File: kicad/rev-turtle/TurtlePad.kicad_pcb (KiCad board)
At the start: 2 copper layers, 57.2 x 63.6 mm, 40 parts, among them J1 USB_IN, J2 AVR-ISP-6, SW1 SW_Push, U1 USBLC6-2SC6, U2 ATMEGA32U4, Y1 16MHz

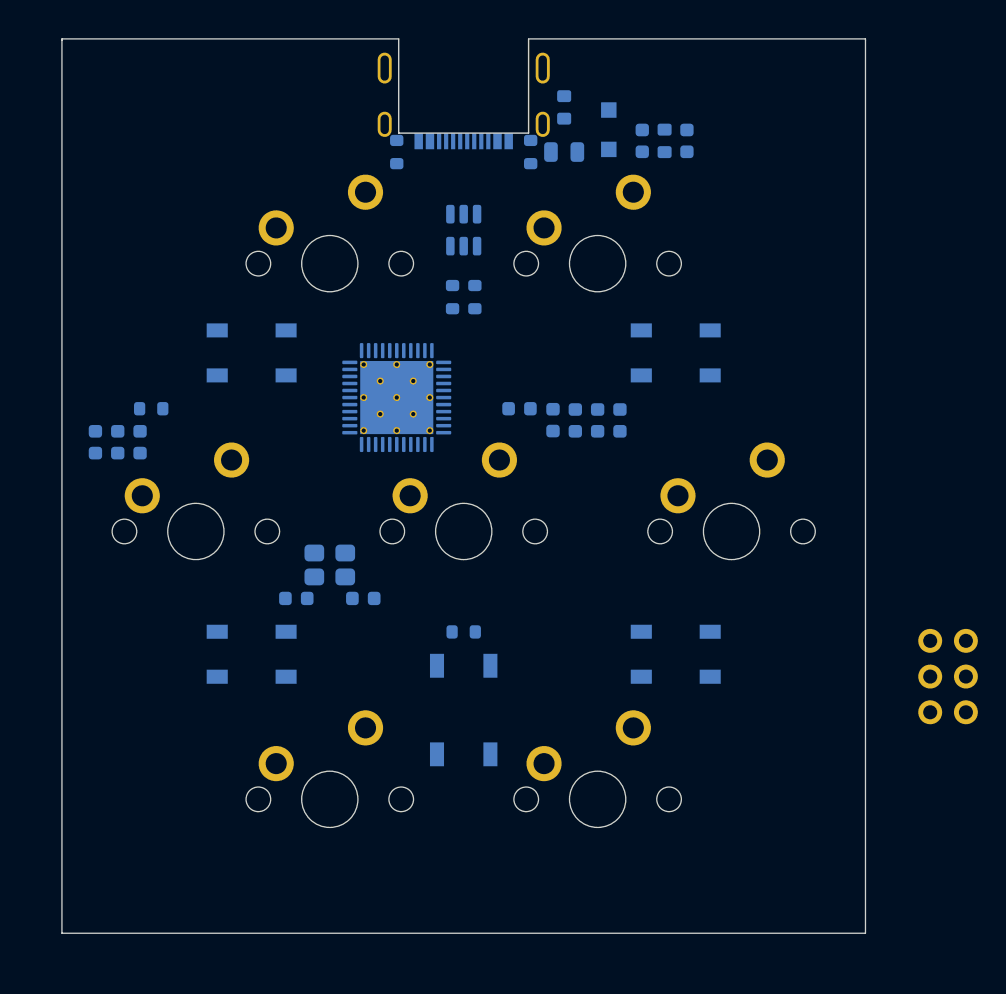
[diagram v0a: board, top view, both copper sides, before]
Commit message: Placed and routed all components on PCB
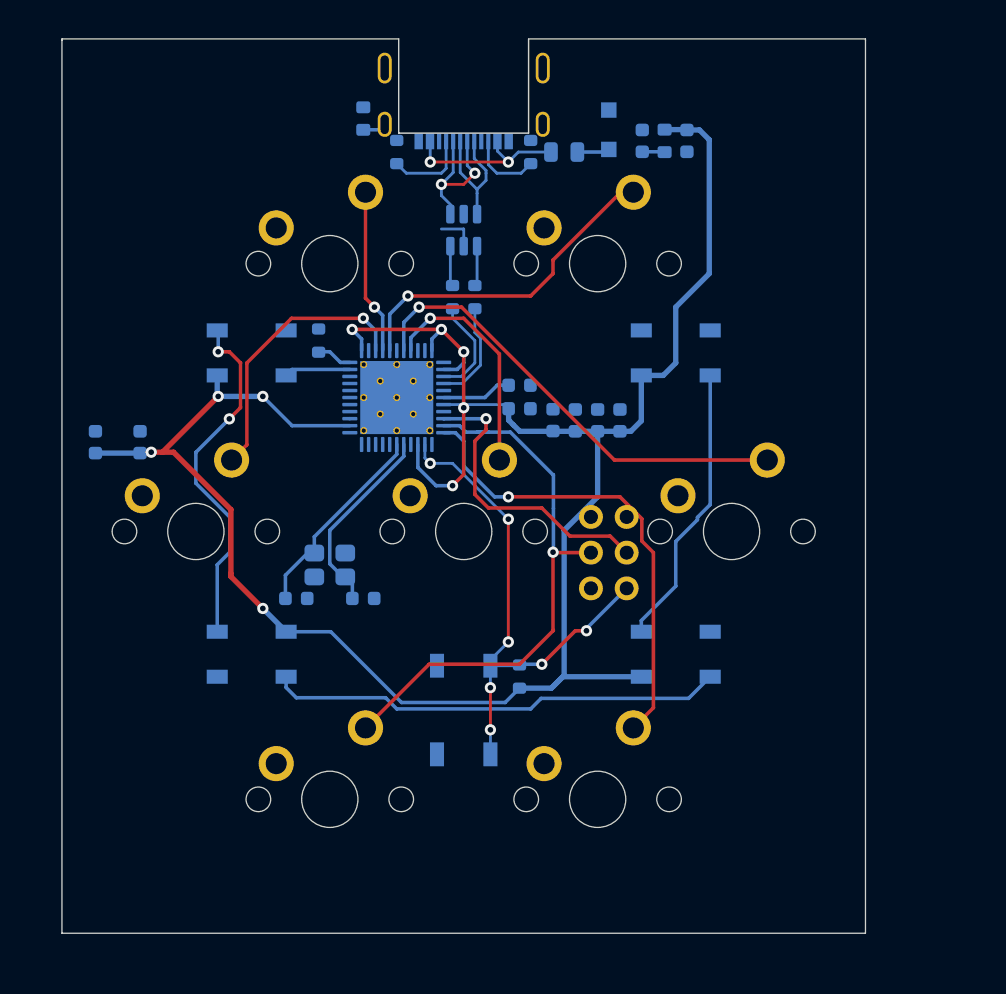
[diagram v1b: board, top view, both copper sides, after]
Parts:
- moved C9 28.9 mm to (131.8, 79.4), turned to 0 degrees
- moved J2 25.7 mm to (138.1, 91.3)
- moved FB2 14.3 mm to (120.7, 60.4)
- moved R6 12.9 mm to (117.5, 76.2), turned to -90 degrees
- moved R5 5.08 mm to (131.8, 100.1), turned to -90 degrees
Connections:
- J2 pad 1: MISO -> MX7
- J2 pad 4: MOSI -> MX6
- U2 pad 10: MOSI -> MX6
- U2 pad 11: MISO -> MX7
- U2 pad 18: MX1 -> unconnected-(U2-Pad18)
- U2 pad 19: MX2 -> unconnected-(U2-Pad19)
- U2 pad 20: MX3 -> SCK
- U2 pad 21: MX4 -> MOSI
- U2 pad 22: MX6 -> unconnected-(U2-Pad22)
- U2 pad 25: MX5 -> MISO
- U2 pad 26: MX7 -> unconnected-(U2-Pad26)
- U2 pad 32: unconnected-(U2-Pad32) -> LED
- U2 pad 36: unconnected-(U2-Pad36) -> MX3
- U2 pad 37: unconnected-(U2-Pad37) -> MX1
- U2 pad 38: unconnected-(U2-Pad38) -> MX2
- U2 pad 40: unconnected-(U2-Pad40) -> MX5
- U2 pad 41: unconnected-(U2-Pad41) -> MX4
- U2 pad 8: LED -> unconnected-(U2-Pad8)
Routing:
- net VCC: track 0.00 -> 157.7 mm, vias 0 -> 9
- net MX6: track 0.00 -> 40.1 mm, vias 0 -> 1
- net RST: track 0.00 -> 38.0 mm, vias 0 -> 7
- net MX7: track 0.00 -> 33.5 mm, vias 0 -> 1
- net MX5: track 0.00 -> 32.8 mm, vias 0 -> 1
- net Net-(RGB2-Pad2): track 0.00 -> 32.5 mm
- net Net-(RGB1-Pad2): track 0.00 -> 25.3 mm, vias 0 -> 2
- net MX2: track 0.00 -> 24.1 mm, vias 0 -> 1
- net SCK: track 0.00 -> 21.2 mm, vias 0 -> 1
- net Net-(RGB3-Pad2): track 0.00 -> 20.3 mm
- net MX3: track 0.00 -> 19.6 mm, vias 0 -> 1
- net MX4: track 0.00 -> 16.4 mm, vias 0 -> 1
- net /VBUS: track 0.00 -> 15.0 mm, vias 0 -> 2
- net Net-(C8-Pad2): track 0.00 -> 14.5 mm
- net Net-(C7-Pad2): track 0.00 -> 13.9 mm
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
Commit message: PCB edge and copper fill
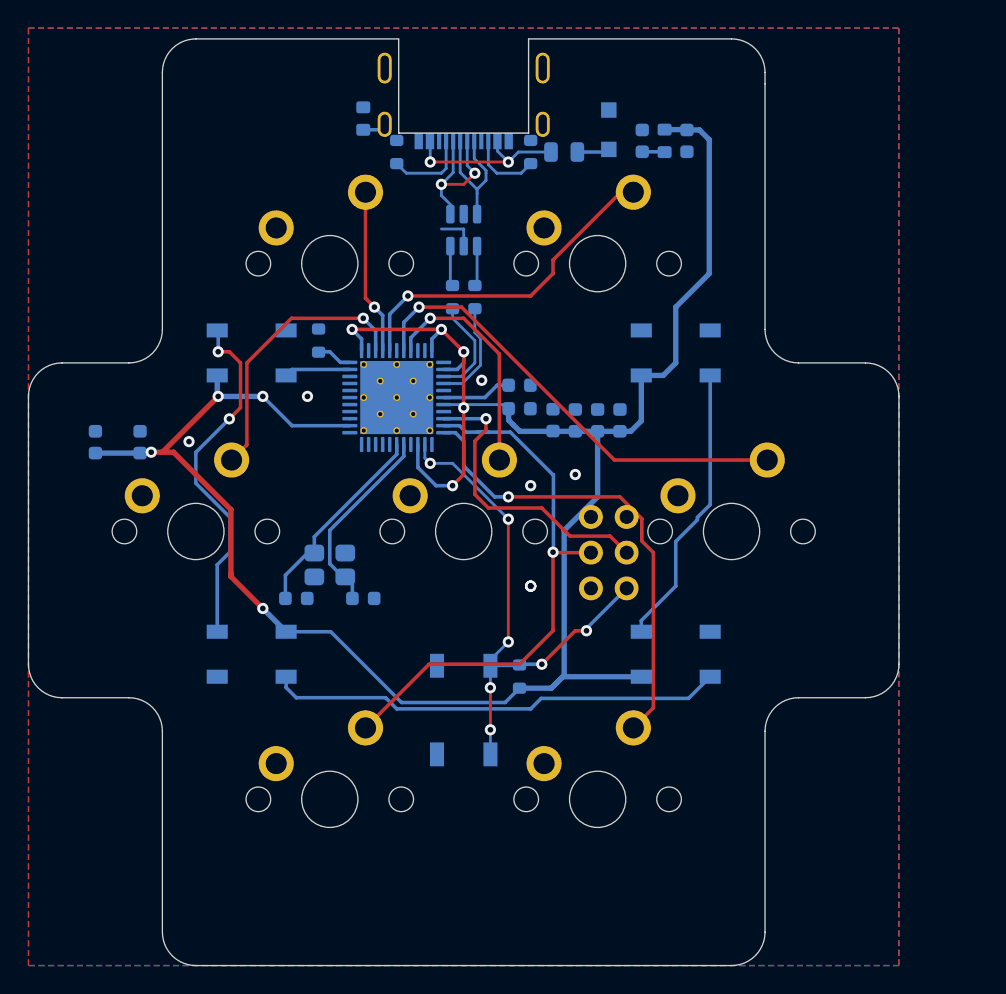
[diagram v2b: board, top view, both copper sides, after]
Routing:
- net GND: vias 0 -> 8
- added copper zone on B.Cu, net GND
- added copper zone on F.Cu, net GND
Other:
- board size 57.2 x 63.6 mm -> 61.9 x 65.9 mm
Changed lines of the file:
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@@
     )
   )
-  (gr_line (start 156.36875 118.350939) (end 99.21875 118.350939) (layer "Edge.Cuts") (width 0.05))
-  (gr_line (start 99.21875 54.742189) (end 99.21875 54.850939) (layer "Edge.Cuts") (width 0.05))
-  (gr_line (start 99.21875 118.350939) (end 99.21875 54.850939) (layer "Edge.Cuts") (width 0.05))
-  (gr_line (start 132.40875 54.742189) (end 156.36875 54.742189) (layer "Edge.Cuts") (width 0.05))
-  (gr_line (start 156.36875 54.850939) (end 156.36875 54.742189) (layer "Edge.Cuts") (width 0.05))
-  (gr_line (start 123.16875 54.742189) (end 99.21875 54.742189) (layer "Edge.Cuts") (width 0.05))
-  (gr_line (start 156.36875 54.850939) (end 156.36875 118.350939) (layer "Edge.Cuts") (width 0.05))
+  (gr_arc (start 156.36875 77.7875) (mid 158.052548 78.484952) (end 158.75 80.16875) (layer "Edge.Cuts") (width 0.05))
+  (gr_arc (start 106.3625 57.123439) (mid 107.059952 55.439641) (end 108.74375 54.742189) (layer "Edge.Cuts") (width 0.05))
+  (gr_arc (start 103.98125 101.6) (mid 105.665048 102.297452) (end 106.3625 103.98125) (layer "Edge.Cuts") (width 0.05))
+  (gr_line (start 149.225 57.94375) (end 149.225 57.123439) (layer "Edge.Cuts") (width 0.05))
+  (gr_arc (start 146.84375 54.742189) (mid 148.527548 55.439641) (end 149.225 57.123439) (layer "Edge.Cuts") (width 0.05))
+  (gr_line (start 156.36875 77.7875) (end 151.60625 77.7875) (layer "Edge.Cuts") (width 0.05))
+  (gr_arc (start 151.60625 77.7875) (mid 149.922452 77.090048) (end 149.225 75.40625) (layer "Edge.Cuts") (width 0.05))
+  (gr_arc (start 99.21875 101.6) (mid 97.534952 100.902548) (end 96.8375 99.21875) (layer "Edge.Cuts") (width 0.05))
+  (gr_line (start 99.21875 101.6) (end 103.98125 101.6) (layer "Edge.Cuts") (width 0.05))
+  (gr_line (start 108.74375 120.65) (end 146.84375 120.65) (layer "Edge.Cuts") (width 0.05))
+  (gr_line (start 106.3625 57.123439) (end 106.3625 75.40625) (layer "Edge.Cuts") (width 0.05))
+  (gr_line (start 149.225 118.26875) (end 149.225 103.98125) (layer "Edge.Cuts") (width 0.05))
+  (gr_line (start 106.3625 103.98125) (end 106.3625 118.26875) (layer "Edge.Cuts") (width 0.05))
+  (gr_line (start 103.98125 77.7875) (end 99.21875 77.7875) (layer "Edge.Cuts") (width 0.05))
+  (gr_line (start 158.75 99.21875) (end 158.75 80.16875) (layer "Edge.Cuts") (width 0.05))
+  (gr_arc (start 158.75 99.21875) (mid 158.052548 100.902548) (end 156.36875 101.6) (layer "Edge.Cuts") (width 0.05))
+  (gr_arc (start 149.225 103.98125) (mid 149.922452 102.297452) (end 151.60625 101.6) (layer "Edge.Cuts") (width 0.05))
+  (gr_arc (start 149.225 118.26875) (mid 148.527548 119.952548) (end 146.84375 120.65) (layer "Edge.Cuts") (width 0.05))
+  (gr_arc (start 96.8375 80.16875) (mid 97.534952 78.484952) (end 99.21875 77.7875) (layer "Edge.Cuts") (width 0.05))
+  (gr_line (start 151.60625 101.6) (end 156.36875 101.6) (layer "Edge.Cuts") (width 0.05))
+  (gr_line (start 123.16875 54.742189) (end 108.74375 54.742189) (layer "Edge.Cuts") (width 0.05))
+  (gr_line (start 96.8375 80.16875) (end 96.8375 99.21875) (layer "Edge.Cuts") (width 0.05))
+  (gr_line (start 149.225 75.40625) (end 149.225 57.94375) (layer "Edge.Cuts") (width 0.05))
+  (gr_arc (start 108.74375 120.65) (mid 107.059952 119.952548) (end 106.3625 118.26875) (layer "Edge.Cuts") (width 0.05))
+  (gr_arc (start 106.3625 75.40625) (mid 105.665048 77.090048) (end 103.98125 77.7875) (layer "Edge.Cuts") (width 0.05))
+  (gr_line (start 132.40875 54.742189) (end 146.84375 54.742189) (layer "Edge.Cuts") (width 0.05))
+  (via (at 132.55625 93.6625) (size 0.8) (drill 0.4) (layers "F.Cu" "B.Cu") (free) (net 2))
+  (via (at 135.73125 85.725) (size 0.8) (drill 0.4) (layers "F.Cu" "B.Cu") (free) (net 2))
+  (via (at 132.55625 93.6625) (size 0.8) (drill 0.4) (layers "F.Cu" "B.Cu") (free) (net 2))
+  (via (at 129.072531 79.023114) (size 0.8) (drill 0.4) (layers "F.Cu" "B.Cu") (free) (net 2))
+  (via (at 108.254941 83.381183) (size 0.8) (drill 0.4) (layers "F.Cu" "B.Cu") (free) (net 2))
+  (via (at 132.55625 93.6625) (size 0.8) (drill 0.4) (layers "F.Cu" "B.Cu") (free) (net 2))
+  (via (at 116.68125 80.16875) (size 0.8) (drill 0.4) (layers "F.Cu" "B.Cu") (free) (net 2))
+  (via (at 132.55625 86.51875) (size 0.8) (drill 0.4) (layers "F.Cu" "B.Cu") (free) (net 2))
   (segment (start 126.20625 75.40625) (end 119.85625 75.40625) (width 0.254) (layer "F.Cu") (net 3))
   (segment (start 106.3625 84.1375) (end 107.15625 84.1375) (width 0.381) (layer "F.Cu") (net 3))
@@
   (segment (start 126.374061 81.75625) (end 129.38125 81.75625) (width 0.254) (layer "B.Cu") (net 38))
   (segment (start 126.36875 81.750939) (end 126.374061 81.75625) (width 0.254) (layer "B.Cu") (net 38))
+  (zone (net 2) (net_name "GND") (layers F&B.Cu) (hatch edge 0.508)
+    (connect_pads (clearance 0.508))
+    (min_thickness 0.254) (filled_areas_thickness no)
+    (fill yes (thermal_gap 0.508) (thermal_bridge_width 0.508))
+    (polygon
+      (pts
+        (xy 158.75 120.65)
+        (xy 96.8375 120.65)
+        (xy 96.8375 53.975)
+        (xy 158.75 53.975)
+      )
+    )
+  )
 )
